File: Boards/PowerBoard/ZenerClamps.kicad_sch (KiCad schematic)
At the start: 24 parts

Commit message: Update Layouts
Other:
- note removed: "parallle this"
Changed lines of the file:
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@@
 	(generator_version "9.0")
 	(paper "A4")
-	(text "parallle this\n"
-		(exclude_from_sim no)
-		(at 74.8662 104.0919 0)
-		(effects
-			(font
-				(size 1.27 1.27)
-			)
-		)
-	)
 	(global_label "PHASE_U"
 		(shape input)

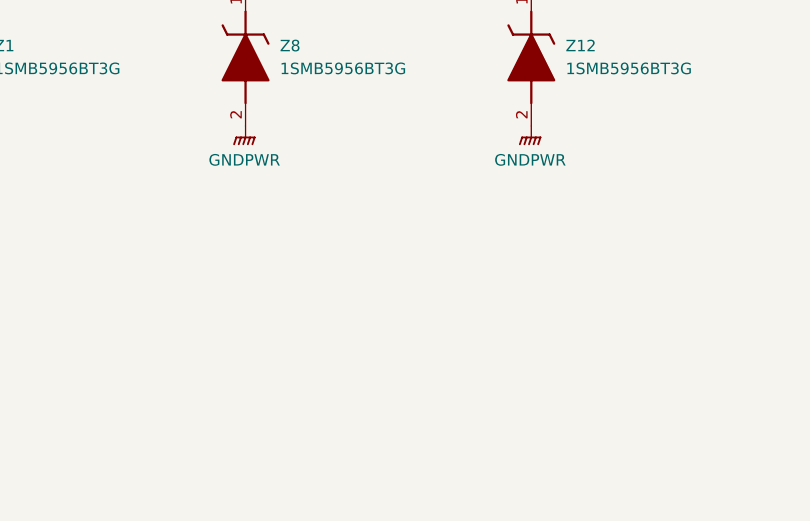
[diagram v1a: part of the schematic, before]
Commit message: Update Dynamic Brake Board
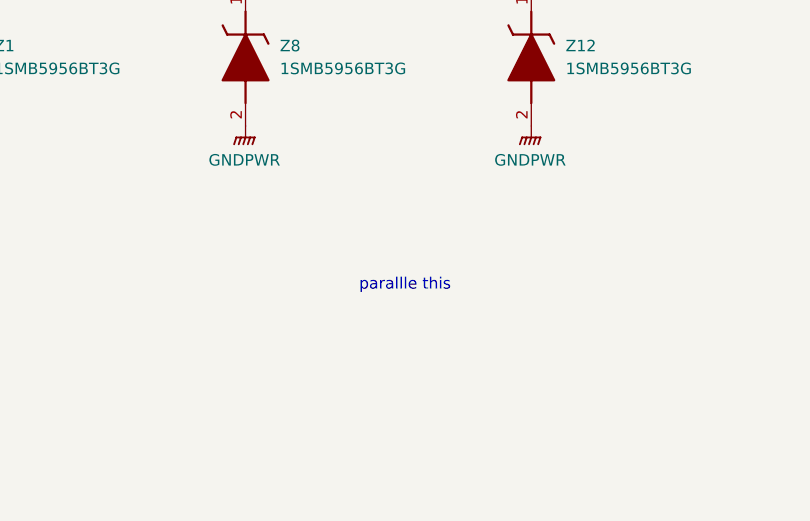
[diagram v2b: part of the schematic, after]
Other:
- note added: "parallle this"
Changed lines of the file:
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@@
 	(generator_version "9.0")
 	(paper "A4")
+	(text "parallle this\n"
+		(exclude_from_sim no)
+		(at 74.8662 104.0919 0)
+		(effects
+			(font
+				(size 1.27 1.27)
+			)
+		)
+	)
 	(global_label "PHASE_U"
 		(shape input)
